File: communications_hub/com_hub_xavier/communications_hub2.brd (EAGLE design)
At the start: 68 x 33 mm, 49 parts, among them CON1 SM04B-GHS-TB, CON2 SM04B-GHS-TB, CON3 SM02B-GHS-TB, CON6 UAVCAN_MICRO, CON7 UAVCAN_MICRO, Q1 DMN5L06K, Q2 DMN5L06K, U1 TCAN1042HVDR, U2 TCAN1042HVDR

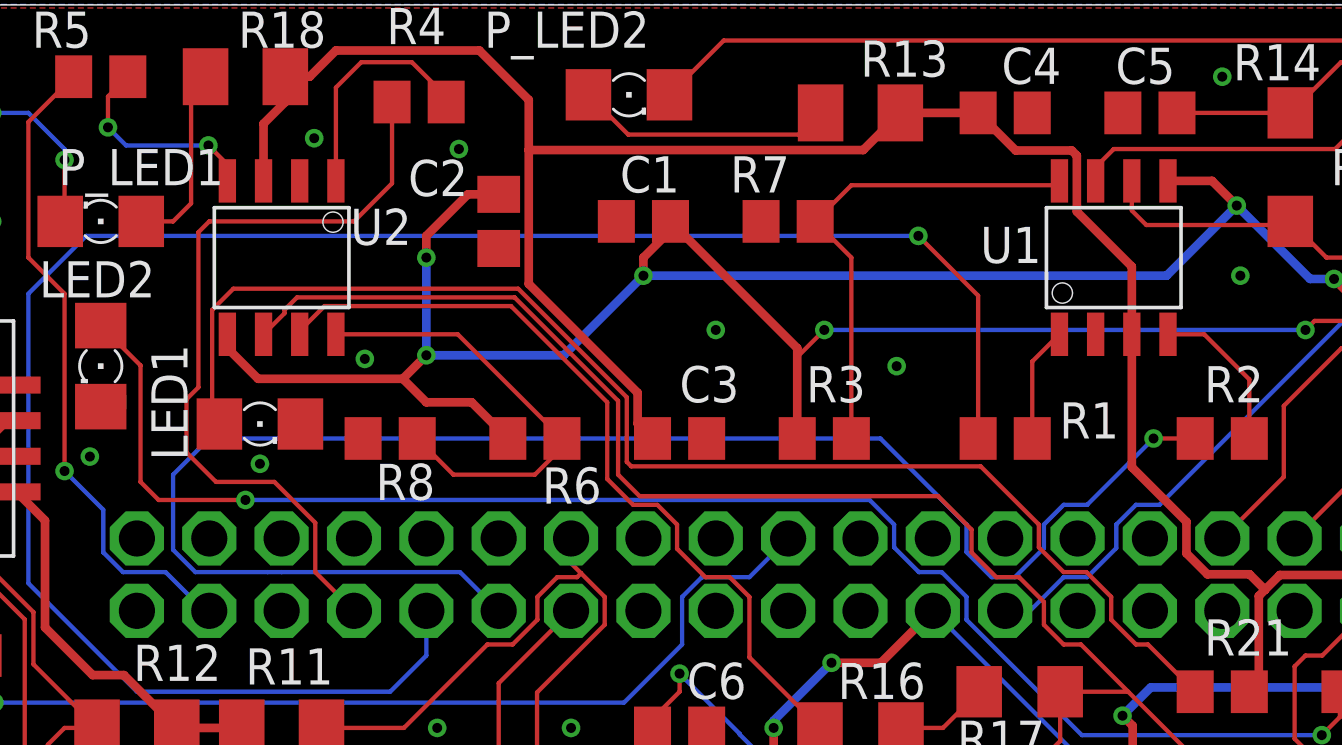
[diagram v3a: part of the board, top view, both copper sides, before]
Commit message: Added a pullup resistor to pin 18 of JP21 for the Go switch. Made slight edits to the BOM to clean up formatting.
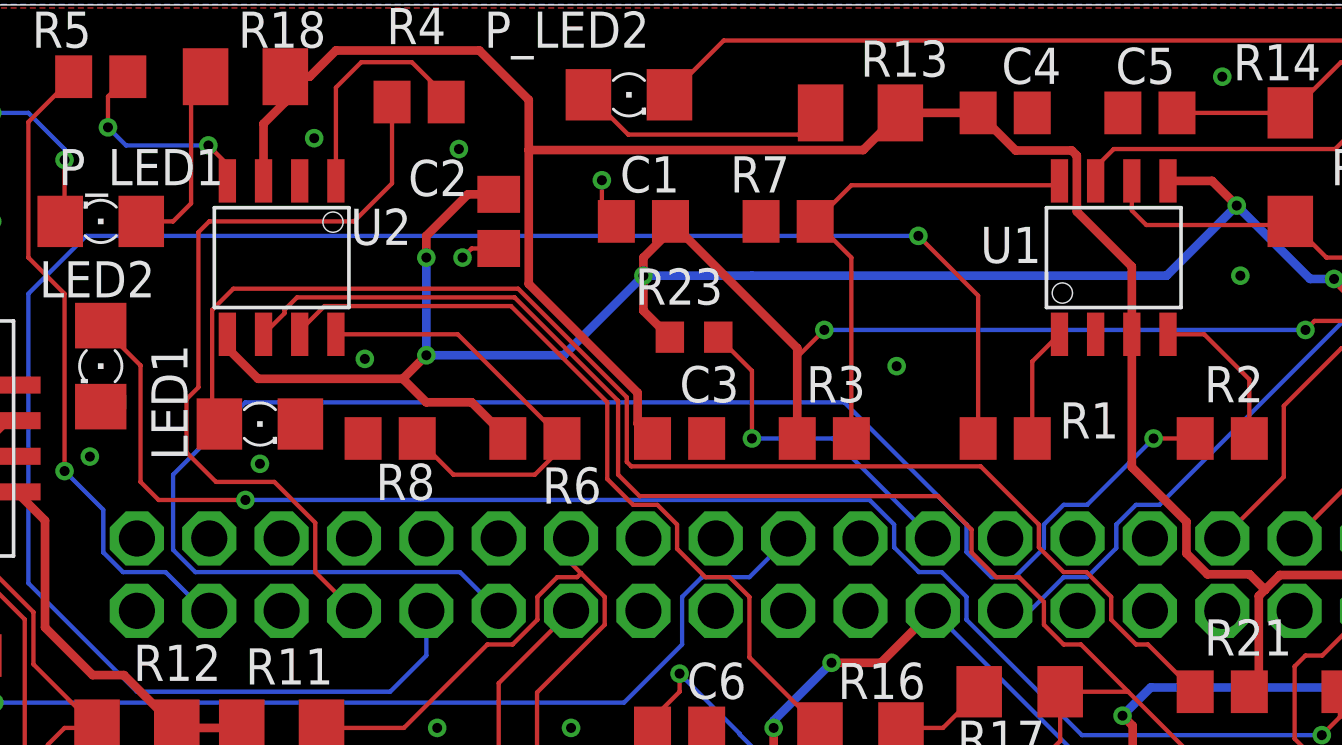
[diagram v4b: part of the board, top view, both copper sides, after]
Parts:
- added R23: 4.7k, audio amplifier example:R0603
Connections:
- new net N$1: JP21.18, R23.1
- net +3V3: now also R23.2
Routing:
- net N$1: track 0.00 -> 11.8 mm, vias 0 -> 1
- net GND: track 3.60 -> 7.08 mm, vias 25 -> 26
- net +3V3: track 204.4 -> 206.9 mm
- net CAN0_RX_T: track 56.4 -> 57.5 mm
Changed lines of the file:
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@@
 <layer number="115" name="ReferenceISLANDS" color="7" fill="1" visible="yes" active="yes"/>
 <layer number="116" name="Patch_BOT" color="9" fill="4" visible="yes" active="yes"/>
+<layer number="117" name="BACKMAAT1" color="7" fill="1" visible="yes" active="yes"/>
 <layer number="118" name="Rect_Pads" color="7" fill="1" visible="yes" active="yes"/>
+<layer number="119" name="KAP_TEKEN" color="7" fill="1" visible="yes" active="yes"/>
+<layer number="120" name="KAP_MAAT1" color="7" fill="1" visible="yes" active="yes"/>
 <layer number="121" name="sName" color="7" fill="1" visible="yes" active="yes"/>
 <layer number="122" name="_bPlace" color="7" fill="1" visible="yes" active="yes"/>
@@
 <layer number="128" name="_bValues" color="7" fill="1" visible="yes" active="yes"/>
 <layer number="129" name="Mask" color="7" fill="1" visible="yes" active="yes"/>
+<layer number="130" name="SMDSTROOK" color="7" fill="1" visible="yes" active="yes"/>
 <layer number="131" name="tAdjust" color="7" fill="1" visible="no" active="yes"/>
 <layer number="132" name="bAdjust" color="7" fill="1" visible="no" active="yes"/>
+<layer number="133" name="bottom_silk" color="7" fill="1" visible="yes" active="yes"/>
+<layer number="134" name="silk_top" color="7" fill="1" visible="yes" active="yes"/>
+<layer number="135" name="silk_bottom" color="7" fill="1" visible="yes" active="yes"/>
+<layer number="136" name="silktop" color="7" fill="1" visible="yes" active="yes"/>
+<layer number="137" name="silkbottom" color="7" fill="1" visible="yes" active="yes"/>
 <layer number="144" name="Drill_legend" color="7" fill="1" visible="yes" active="yes"/>
+<layer number="145" name="DrillLegend_01-16" color="7" fill="1" visible="yes" active="yes"/>
+<layer number="146" name="DrillLegend_01-20" color="7" fill="1" visible="yes" active="yes"/>
 <layer number="150" name="Notes" color="7" fill="1" visible="no" active="yes"/>
 <layer number="151" name="HeatSink" color="7" fill="1" visible="yes" active="yes"/>
@@
 <layer number="154" name="FabDoc2" color="2" fill="1" visible="no" active="no"/>
 <layer number="155" name="FabDoc3" color="7" fill="15" visible="no" active="no"/>
+<layer number="166" name="AntennaArea" color="7" fill="1" visible="yes" active="yes"/>
+<layer number="168" name="4mmHeightArea" color="7" fill="1" visible="yes" active="yes"/>
 <layer number="199" name="Contour" color="7" fill="1" visible="yes" active="yes"/>
 <layer number="200" name="200bmp" color="1" fill="10" visible="yes" active="yes"/>
@@
 <element name="CON6" library="SPEAR-general" package="SM04B-GHS-TB" value="UAVCAN_MICRO" x="57.15" y="5.08" smashed="yes"/>
 <element name="CON7" library="SPEAR-general" package="SM04B-GHS-TB" value="UAVCAN_MICRO" x="46.99" y="5.08" smashed="yes"/>
+<element name="R23" library="audio amplifier example" library_urn="urn:adsk.eagle:library:970892" package="R0603" package3d_urn="urn:adsk.eagle:package:970938/2" value="4.7k" x="29.718" y="21.336" smashed="yes" rot="R180">
+<attribute name="NAME" x="30.734" y="23.749" size="1.27" layer="25" rot="R180"/>
+</element>
 </elements>
 <signals>
@@
 <via x="3.81" y="7.62" extent="1-16" drill="0.35"/>
 <via x="16.383" y="28.321" extent="1-16" drill="0.35"/>
-<via x="30.48" y="21.59" extent="1-16" drill="0.35"/>
 <via x="48.895" y="23.495" extent="1-16" drill="0.35"/>
 <via x="60.96" y="30.48" extent="1-16" drill="0.35"/>
@@
 <wire x1="56.96" y1="22.795" x2="57.022" y2="22.733" width="0.1524" layer="1"/>
 <via x="58.928" y="22.733" extent="1-16" drill="0.35"/>
+<wire x1="22.86" y1="24.45" x2="22.86" y2="24.463" width="0.1524" layer="1"/>
+<wire x1="22.86" y1="24.45" x2="22.803" y2="24.393" width="0.1524" layer="1"/>
+<wire x1="22.86" y1="24.336" x2="22.86" y2="24.082" width="0.1524" layer="1"/>
+<wire x1="22.86" y1="24.336" x2="22.803" y2="24.393" width="0.1524" layer="1"/>
+<wire x1="26.482" y1="26.845" x2="26.482" y2="25.908" width="0.1524" layer="1"/>
+<wire x1="26.99" y1="25.4" x2="26.482" y2="25.908" width="0.1524" layer="1"/>
+<via x="26.482" y="26.845" extent="1-16" drill="0.35"/>
+<wire x1="22.86" y1="24.45" x2="21.91" y2="24.45" width="0.1524" layer="1"/>
+<wire x1="21.91" y1="24.45" x2="21.59" y2="24.13" width="0.1524" layer="1"/>
+<via x="21.59" y="24.13" extent="1-16" drill="0.35"/>
 </signal>
 <signal name="+3V3">
@@
 <via x="48.768" y="25.956" extent="1-16" drill="0.35"/>
 <wire x1="48.768" y1="25.956" x2="46.307" y2="23.495" width="0.3048" layer="16"/>
-<wire x1="46.307" y1="23.495" x2="27.94" y2="23.495" width="0.3048" layer="16"/>
+<wire x1="46.307" y1="23.495" x2="31.75" y2="23.495" width="0.3048" layer="16"/>
 <via x="52.184846875" y="23.380153125" extent="1-16" drill="0.35"/>
+<wire x1="31.75" y1="23.495" x2="27.94" y2="23.495" width="0.3048" layer="16"/>
 <wire x1="52.184846875" y1="23.380153125" x2="53.6575" y2="21.9075" width="0.3048" layer="1"/>
 <wire x1="53.6575" y1="21.9075" x2="54.0152" y2="21.5498" width="0.3048" layer="1"/>
@@
 <wire x1="11.60895" y1="2.54" x2="12.91375" y2="1.2352" width="0.3048" layer="1"/>
 <wire x1="14.76625" y1="1.2352" x2="16.07105" y2="2.54" width="0.3048" layer="1"/>
+<contactref element="R23" pad="2"/>
+<wire x1="27.94" y1="23.495" x2="27.94" y2="22.264" width="0.3048" layer="1"/>
+<wire x1="27.94" y1="22.264" x2="28.868" y2="21.336" width="0.3048" layer="1"/>
 </signal>
 <signal name="CAN0_RX_T">
@@
 <wire x1="39.2811" y1="13.79184375" x2="39.2811" y2="14.75923125" width="0.1524" layer="16"/>
 <wire x1="40.16184375" y1="12.9111" x2="39.2811" y2="13.79184375" width="0.1524" layer="16"/>
-<wire x1="14.75076875" y1="13.0889" x2="15.24" y2="13.0889" width="0.1524" layer="16"/>
-<wire x1="15.24" y1="13.0889" x2="21.5011" y2="13.0889" width="0.1524" layer="16"/>
+<wire x1="12.21076875" y1="13.0889" x2="21.5011" y2="13.0889" width="0.1524" layer="16"/>
 <wire x1="21.5011" y1="13.0889" x2="22.86" y2="11.73" width="0.1524" layer="16"/>
-<wire x1="36.26033125" y1="17.78" x2="12.7" y2="17.78" width="0.1524" layer="16"/>
-<wire x1="12.7" y1="17.78" x2="11.43" y2="16.51" width="0.1524" layer="16"/>
+<wire x1="34.99033125" y1="19.05" x2="13.97" y2="19.05" width="0.1524" layer="16"/>
+<wire x1="13.97" y1="19.05" x2="11.43" y2="16.51" width="0.1524" layer="16"/>
 <wire x1="11.43" y1="13.86966875" x2="12.21076875" y2="13.0889" width="0.1524" layer="16"/>
-<wire x1="12.21076875" y1="13.0889" x2="14.75076875" y2="13.0889" width="0.1524" layer="16"/>
-<wire x1="39.2811" y1="14.75923125" x2="36.26033125" y2="17.78" width="0.1524" layer="16"/>
+<wire x1="39.2811" y1="14.75923125" x2="34.99033125" y2="19.05" width="0.1524" layer="16"/>
 <wire x1="11.43" y1="16.51" x2="11.43" y2="13.86966875" width="0.1524" layer="16"/>
 </signal>
@@
 <wire x1="52.39" y1="8.001" x2="51.755" y2="7.366" width="0.1524" layer="1"/>
 </signal>
+<signal name="N$1">
+<contactref element="JP21" pad="18"/>
+<contactref element="R23" pad="1"/>
+<wire x1="30.568" y1="21.336" x2="31.75" y2="20.154" width="0.1524" layer="1"/>
+<wire x1="31.75" y1="20.154" x2="31.75" y2="17.78" width="0.1524" layer="1"/>
+<via x="31.75" y="17.78" extent="1-16" drill="0.35"/>
+<wire x1="31.75" y1="17.78" x2="34.59" y2="17.78" width="0.1524" layer="16"/>
+<wire x1="34.59" y1="17.78" x2="38.1" y2="14.27" width="0.1524" layer="16"/>
+</signal>
 </signals>
